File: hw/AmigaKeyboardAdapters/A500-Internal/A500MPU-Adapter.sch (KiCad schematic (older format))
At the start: 15 parts, among them P1 CONN_01X08, P2 CONN_01X08, P3 CONN_02X03, P4 CONN_01X02, P5 CONN_01X02

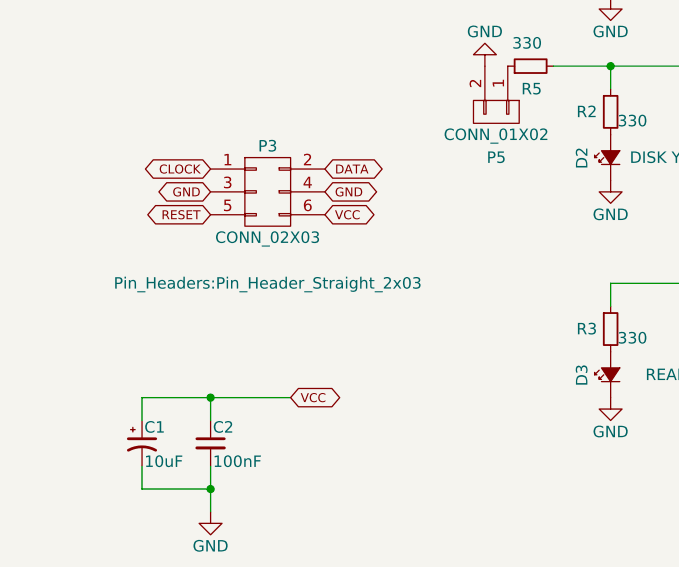
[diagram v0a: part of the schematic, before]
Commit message: added the idc 2x3 box
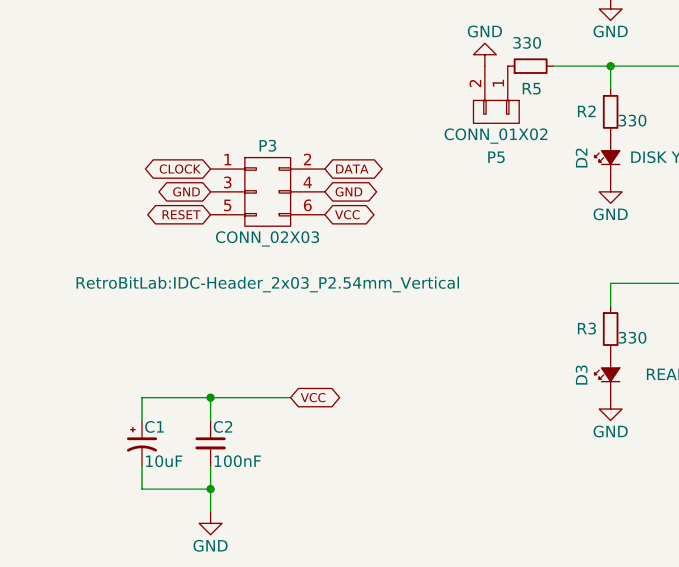
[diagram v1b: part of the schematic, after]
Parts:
- P3: footprint Pin_Headers:Pin_Header_Straight_2x03 -> RetroBitLab:IDC-Header_2x03_P2.54mm_Vertical
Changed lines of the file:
@@
 LIBS:valves
 LIBS:AmigaComponents
+LIBS:4xxx
+LIBS:4xxx_IEEE
+LIBS:74xGxx
+LIBS:74xx_IEEE
+LIBS:Amplifier_Audio
+LIBS:Amplifier_Buffer
+LIBS:Amplifier_Current
+LIBS:Amplifier_Difference
+LIBS:Amplifier_Instrumentation
+LIBS:Amplifier_Operational
+LIBS:Amplifier_Video
+LIBS:Analog
+LIBS:Analog_ADC
+LIBS:Analog_DAC
+LIBS:Analog_Switch
+LIBS:Audio
+LIBS:Battery_Management
+LIBS:Comparator
+LIBS:Connector
+LIBS:Connector_Generic
+LIBS:Connector_Generic_MountingPin
+LIBS:Connector_Generic_Shielded
+LIBS:Converter_ACDC
+LIBS:Converter_DCDC
+LIBS:CPLD_Altera
+LIBS:CPLD_Xilinx
+LIBS:CPU
+LIBS:CPU_NXP_6800
+LIBS:CPU_NXP_68000
+LIBS:CPU_PowerPC
+LIBS:Device
+LIBS:Diode
+LIBS:Diode_Bridge
+LIBS:Diode_Laser
+LIBS:Display_Character
+LIBS:Display_Graphic
+LIBS:Driver_Display
+LIBS:Driver_FET
+LIBS:Driver_LED
+LIBS:Driver_Motor
+LIBS:Driver_Relay
+LIBS:DSP_AnalogDevices
+LIBS:DSP_Freescale
+LIBS:DSP_Microchip_DSPIC33
+LIBS:DSP_Motorola
+LIBS:DSP_Texas
+LIBS:Fiber_Optic
+LIBS:Filter
+LIBS:FPGA_Lattice
+LIBS:FPGA_Microsemi
+LIBS:FPGA_Xilinx
+LIBS:FPGA_Xilinx_Artix7
+LIBS:FPGA_Xilinx_Kintex7
+LIBS:FPGA_Xilinx_Spartan6
+LIBS:FPGA_Xilinx_Virtex5
+LIBS:FPGA_Xilinx_Virtex6
+LIBS:FPGA_Xilinx_Virtex7
+LIBS:ft232rl
+LIBS:GPU
+LIBS:Graphic
+LIBS:Interface
+LIBS:Interface_CAN_LIN
+LIBS:Interface_CurrentLoop
+LIBS:Interface_Ethernet
+LIBS:Interface_Expansion
+LIBS:Interface_HID
+LIBS:Interface_LineDriver
+LIBS:Interface_Optical
+LIBS:Interface_Telecom
+LIBS:Interface_UART
+LIBS:Interface_USB
+LIBS:Isolator
+LIBS:Isolator_Analog
+LIBS:Jumper
+LIBS:LED
+LIBS:Logic_LevelTranslator
+LIBS:Logic_Programmable
+LIBS:MCU_AnalogDevices
+LIBS:MCU_Cypress
+LIBS:MCU_Espressif
+LIBS:MCU_Intel
+LIBS:MCU_Microchip_8051
+LIBS:MCU_Microchip_ATmega
+LIBS:MCU_Microchip_ATtiny
+LIBS:MCU_Microchip_AVR
+LIBS:MCU_Microchip_PIC10
+LIBS:MCU_Microchip_PIC12
+LIBS:MCU_Microchip_PIC16
+LIBS:MCU_Microchip_PIC18
+LIBS:MCU_Microchip_PIC24
+LIBS:MCU_Microchip_PIC32
+LIBS:MCU_Microchip_SAMD
+LIBS:MCU_Microchip_SAME
+LIBS:MCU_Microchip_SAML
+LIBS:MCU_Module
+LIBS:MCU_Nordic
+LIBS:MCU_NXP_ColdFire
+LIBS:MCU_NXP_HC11
+LIBS:MCU_NXP_HC12
+LIBS:MCU_NXP_HCS12
+LIBS:MCU_NXP_Kinetis
+LIBS:MCU_NXP_LPC
+LIBS:MCU_NXP_MAC7100
+LIBS:MCU_NXP_MCore
+LIBS:MCU_NXP_S08
+LIBS:MCU_Parallax
+LIBS:MCU_SiFive
+LIBS:MCU_SiliconLabs
+LIBS:MCU_ST_STM8
+LIBS:MCU_ST_STM32F0
+LIBS:MCU_ST_STM32F1
+LIBS:MCU_ST_STM32F2
+LIBS:MCU_ST_STM32F3
+LIBS:MCU_ST_STM32F4
+LIBS:MCU_ST_STM32F7
+LIBS:MCU_ST_STM32H7
+LIBS:MCU_ST_STM32L0
+LIBS:MCU_ST_STM32L1
+LIBS:MCU_ST_STM32L4
+LIBS:MCU_ST_STM32L4+
+LIBS:MCU_Texas
+LIBS:MCU_Texas_MSP430
+LIBS:Mechanical
+LIBS:Memory_Controller
+LIBS:Memory_EEPROM
+LIBS:Memory_EPROM
+LIBS:Memory_Flash
+LIBS:Memory_NVRAM
+LIBS:Memory_RAM
+LIBS:Memory_ROM
+LIBS:Memory_UniqueID
+LIBS:Motor
+LIBS:Oscillator
+LIBS:Potentiometer_Digital
+LIBS:Power_Management
+LIBS:Power_Protection
+LIBS:Power_Supervisor
+LIBS:pspice
+LIBS:Reference_Current
+LIBS:Reference_Voltage
+LIBS:Regulator_Controller
+LIBS:Regulator_Current
+LIBS:Regulator_Linear
+LIBS:Regulator_SwitchedCapacitor
+LIBS:Regulator_Switching
+LIBS:Relay
+LIBS:Relay_SolidState
+LIBS:RF
+LIBS:RF_AM_FM
+LIBS:RF_Amplifier
+LIBS:RF_Bluetooth
+LIBS:RF_GPS
+LIBS:RF_GSM
+LIBS:RF_Mixer
+LIBS:RF_Module
+LIBS:RF_RFID
+LIBS:RF_Switch
+LIBS:RF_WiFi
+LIBS:RF_ZigBee
+LIBS:Security
+LIBS:Sensor
+LIBS:Sensor_Audio
+LIBS:Sensor_Current
+LIBS:Sensor_Gas
+LIBS:Sensor_Humidity
+LIBS:Sensor_Magnetic
+LIBS:Sensor_Motion
+LIBS:Sensor_Optical
+LIBS:Sensor_Pressure
+LIBS:Sensor_Proximity
+LIBS:Sensor_Temperature
+LIBS:Sensor_Touch
+LIBS:Sensor_Voltage
+LIBS:Switch
+LIBS:Timer
+LIBS:Timer_PLL
+LIBS:Timer_RTC
+LIBS:Transformer
+LIBS:Transistor_Array
+LIBS:Transistor_BJT
+LIBS:Transistor_FET
+LIBS:Transistor_IGBT
+LIBS:Triac_Thyristor
+LIBS:Valve
+LIBS:Video
 LIBS:A500MPU-Adapter-cache
 EELAYER 25 0
@@
 F 0 "P3" H 4400 3650 50  0000 C CNN
 F 1 "CONN_02X03" H 4400 3250 50  0000 C CNN
-F 2 "Pin_Headers:Pin_Header_Straight_2x03" H 4400 3050 50  0000 C CNN
+F 2 "RetroBitLab:IDC-Header_2x03_P2.54mm_Vertical" H 4400 3050 50  0000 C CNN
 F 3 "" H 4400 2250 50  0000 C CNN
 	1    4400 3450

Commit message: From KiCAD 4 to KiCAD 5
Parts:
- removed D1: LED GREEN, SMD_Packages:SMD-1206_Pol, symbol Led_Small
- removed D2: DISK YELLOW, SMD_Packages:SMD-1206_Pol, symbol Led_Small
- removed D3: READY RED, SMD_Packages:SMD-1206_Pol, symbol Led_Small
- removed P1: CONN_01X08, Pin_Headers:Pin_Header_Straight_1x08, symbol CONN_01X08
- removed P2: CONN_01X08, Socket_Strips:Socket_Strip_Straight_1x08, symbol CONN_01X08
- removed P3: CONN_02X03, RetroBitLab:IDC-Header_2x03_P2.54mm_Vertical, symbol CONN_02X03
- removed P4, P5: CONN_01X02, Pin_Headers:Pin_Header_Straight_1x02, symbol CONN_01X02
- removed R1, R3, R4, R5: 330, Resistors_SMD:R_1206_HandSoldering, symbol R_Small
- added D1: POWER ORANGE, LED_SMD:LED_1206_3216Metric_Pad1.42x1.75mm_HandSolder, symbol Device:LED
- added D2: FLOPPY GREEN, LED_SMD:LED_1206_3216Metric_Pad1.42x1.75mm_HandSolder, symbol Device:LED
- added D3: READY RED, LED_SMD:LED_1206_3216Metric_Pad1.42x1.75mm_HandSolder, symbol Device:LED
- added P1: Conn_01x08, Connector_PinHeader_2.54mm:PinHeader_1x08_P2.54mm_Vertical, symbol Connector_Generic:Conn_01x08
- added P2: Conn_01x08, Connector_PinSocket_2.54mm:PinSocket_1x08_P2.54mm_Vertical, symbol Connector_Generic:Conn_01x08
- added P3: Conn_02x03, Connector_IDC:IDC-Header_2x03_P2.54mm_Vertical, symbol Connector_Generic:Conn_02x03_Odd_Even
- added P4, P5: Conn_01x02, Connector_PinHeader_2.54mm:PinHeader_1x02_P2.54mm_Vertical, symbol Connector_Generic:Conn_01x02
- added R1, R3, R4, R5: 330R, Resistor_SMD:R_1206_3216Metric_Pad1.30x1.75mm_HandSolder, symbol Device:R_Small
- C1: footprint SMD_Packages:SMD-1206_Pol -> Capacitor_Tantalum_SMD:CP_EIA-3216-12_Kemet-S_Pad1.58x1.35mm_HandSolder; symbol CP1_Small -> Device:CP1_Small; LCSC (none) -> C108529
- C2: footprint Capacitors_SMD:C_1206_HandSoldering -> Capacitor_SMD:C_1206_3216Metric_Pad1.33x1.80mm_HandSolder; symbol C_Small -> Device:C_Small; LCSC (none) -> C24497
- R2: value 330 -> 330R; footprint Resistors_SMD:R_1206_HandSoldering -> Resistor_SMD:R_1206_3216Metric_Pad1.30x1.75mm_HandSolder; symbol R_Small -> Device:R_Small; LCSC (none) -> C245520
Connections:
- net INUSE is gone; now on net VCC: R2.1
- net CLOCK: now also P1.1 (Pin_1), P2.1 (Pin_1), P3.1 (Pin_1)
- net DATA: now also P1.2 (Pin_2), P2.2 (Pin_2), P3.2 (Pin_2)
- net GND: now also D1.1 (K), D2.1 (K), D3.1 (K), P1.6 (Pin_6), P2.6 (Pin_6), P3.3 (Pin_3), P3.4 (Pin_4), P4.2 (Pin_2), P5.2 (Pin_2)
- net RESET: now also P1.3 (Pin_3), P2.3 (Pin_3), P3.5 (Pin_5)
- net STATUS: now also P1.7 (Pin_7), P2.7 (Pin_7), R1.1, R4.1
- net VCC: now also P1.4 (Pin_4), P1.8 (Pin_8), P2.4 (Pin_4), P2.8 (Pin_8), P3.6 (Pin_6), R3.1, R5.1
- net at R2.2: now also D2.2 (A)
- new net: P4.1 (Pin_1), R4.2
- new net: P5.1 (Pin_1), R5.2
- new net: D3.2 (A), R3.2
- new net: D1.2 (A), R1.2
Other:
- moved on the sheet: R2
